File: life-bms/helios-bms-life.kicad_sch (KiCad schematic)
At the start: 55 parts, among them J1 Outboard, J2 Debug, J3 Output, J4 Battery, Q1 SSM6J507NU, Q2 Q_Dual_NMOS_PMOS_S1G1D2S2G2D1, Q3 PMOS, U1 TPSM861253, U2 BQ25306, U3 STM32L011F4Ux, U4 THVD1400D, U5 SIP32434

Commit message: oops screwed up power net labels
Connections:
- net +12V: no longer Q2.4 (S), Q3.3 (D), R17.1
- net VIN: now also Q2.4 (S), Q3.3 (D), R17.1
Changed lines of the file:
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@@
-	)
-	(symbol
-		(lib_id "power:+12V")
-		(at 113.03 125.73 0)
-		(unit 1)
-		(body_style 1)
-		(exclude_from_sim no)
-		(in_bom yes)
-		(on_board yes)
-		(in_pos_files yes)
-		(dnp no)
-		(fields_autoplaced yes)
-		(property "Reference" "#PWR035"
-			(at 113.03 129.54 0)
-			(hide yes)
-			(show_name no)
-			(do_not_autoplace no)
-			(effects
-				(font
-					(size 1.27 1.27)
-				)
-			)
-		)
-		(property "Value" "+12V"
-			(at 113.03 120.65 0)
-			(show_name no)
-			(do_not_autoplace no)
-			(effects
-				(font
-					(size 1.27 1.27)
-				)
-			)
-		)
-		(property "Footprint" ""
-			(at 113.03 125.73 0)
-			(hide yes)
-			(show_name no)
-			(do_not_autoplace no)
-			(effects
-				(font
-					(size 1.27 1.27)
-				)
-			)
-		)
-		(property "Datasheet" ""
-			(at 113.03 125.73 0)
-			(hide yes)
-			(show_name no)
-			(do_not_autoplace no)
-			(effects
-				(font
-					(size 1.27 1.27)
-				)
-			)
-		)
-		(property "Description" "Power symbol creates a global label with name \"+12V\""
-			(at 113.03 125.73 0)
-			(hide yes)
-			(show_name no)
-			(do_not_autoplace no)
-			(effects
-				(font
-					(size 1.27 1.27)
-				)
-			)
-		)
-		(pin "1"
-		)
-		(instances
-			(project "helios-bms-life"
-				(path "/e63e39d7-6ac0-4ffd-8aa3-1841a4541b55"
-					(reference "#PWR035")
-					(unit 1)
-				)
-			)
-		)
 	)
 	(symbol
@@
 					(unit 1)
 				)
+			)
+		)
+	)
+	(symbol
+		(lib_id "power:VBUS")
+		(at 113.03 125.73 0)
+		(unit 1)
+		(body_style 1)
+		(exclude_from_sim no)
+		(in_bom yes)
+		(on_board yes)
+		(in_pos_files yes)
+		(dnp no)
+		(property "Reference" "#PWR035"
+			(at 113.03 129.54 0)
+			(hide yes)
+			(show_name no)
+			(do_not_autoplace no)
+			(effects
+				(font
+					(size 1.27 1.27)
+				)
+			)
+		)
+		(property "Value" "VSYS"
+			(at 113.03 122.174 0)
+			(show_name no)
+			(do_not_autoplace no)
+			(effects
+				(font
+					(size 1.27 1.27)
+				)
+			)
+		)
+		(property "Footprint" ""
+			(at 113.03 125.73 0)
+			(hide yes)
+			(show_name no)
+			(do_not_autoplace no)
+			(effects
+				(font
+					(size 1.27 1.27)
+				)
+			)
+		)
+		(property "Datasheet" ""
+			(at 113.03 125.73 0)
+			(hide yes)
+			(show_name no)
+			(do_not_autoplace no)
+			(effects
+				(font
+					(size 1.27 1.27)
+				)
+			)
+		)
+		(property "Description" "Power symbol creates a global label with name \"VBUS\""
+			(at 113.03 125.73 0)
+			(hide yes)
+			(show_name no)
+			(do_not_autoplace no)
+			(effects
+				(font
+					(size 1.27 1.27)
+				)
+			)
+		)
+		(pin "1"
+		)
+		(instances
+			(project "helios-bms-life"
+				(path "/e63e39d7-6ac0-4ffd-8aa3-1841a4541b55"
+					(reference "#PWR035")
+					(unit 1)
+				)

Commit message: satellite boards done
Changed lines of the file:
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@@
 	)
 	(junction
+		(at 36.83 40.64)
+		(diameter 0)
+		(color 0 0 0 0)
+	)
+	(junction
 		(at 170.18 41.91)
 		(diameter 0)
@@
 	)
 	(junction
+		(at 148.59 48.26)
+		(diameter 0)
+		(color 0 0 0 0)
+	)
+	(junction
 		(at 99.06 102.87)
 		(diameter 0)
@@
 	)
 	(junction
+		(at 19.05 113.03)
+		(diameter 0)
+		(color 0 0 0 0)
+	)
+	(junction
 		(at 36.83 29.21)
 		(diameter 0)
@@
 	)
 	(junction
+		(at 148.59 41.91)
+		(diameter 0)
+		(color 0 0 0 0)
+	)
+	(junction
 		(at 68.58 24.13)
 		(diameter 0)
@@
 	)
 	(junction
+		(at 21.59 24.13)
+		(diameter 0)
+		(color 0 0 0 0)
+	)
+	(junction
 		(at 45.72 130.81)
 		(diameter 0)
@@
 	)
 	(junction
+		(at 96.52 144.78)
+		(diameter 0)
+		(color 0 0 0 0)
+	)
+	(junction
 		(at 30.48 24.13)
 		(diameter 0)
@@
 	)
 	(junction
+		(at 45.72 53.34)
+		(diameter 0)
+		(color 0 0 0 0)
+	)
+	(junction
 		(at 30.48 58.42)
 		(diameter 0)
@@
 		(color 0 0 0 0)
 	)
-	(junction
-		(at 144.78 48.26)
-		(diameter 0)
-		(color 0 0 0 0)
-	)
 	(no_connect
 		(at 31.75 86.36)
@@
 	(wire
 		(pts
-			(xy 30.48 22.86) (xy 30.48 24.13)
+			(xy 21.59 22.86) (xy 21.59 24.13)
 		)
 		(stroke
@@
 	(wire
 		(pts
-			(xy 31.75 111.76) (xy 31.75 113.03)
+			(xy 19.05 111.76) (xy 19.05 113.03)
 		)
 		(stroke
@@
 	(wire
 		(pts
+			(xy 45.72 53.34) (xy 44.45 53.34)
+		)
+		(stroke
+			(width 0)
+			(type default)
+		)
+	)
+	(wire
+		(pts
 			(xy 129.54 90.17) (xy 130.81 90.17)
 		)
@@
 	(wire
 		(pts
+			(xy 148.59 41.91) (xy 161.29 41.91)
+		)
+		(stroke
+			(width 0)
+			(type default)
+		)
+	)
+	(wire
+		(pts
 			(xy 20.32 130.81) (xy 20.32 133.35)
 		)
@@
 	(wire
 		(pts
-			(xy 19.05 113.03) (xy 31.75 113.03)
-		)
-		(stroke
-			(width 0)
-			(type default)
-		)
-	)
-	(wire
-		(pts
 			(xy 91.44 100.33) (xy 91.44 102.87)
 		)
@@
 	(wire
 		(pts
-			(xy 52.07 40.64) (xy 71.12 40.64)
-		)
-		(stroke
-			(width 0)
-			(type default)
-		)
-	)
-	(wire
-		(pts
 			(xy 35.56 175.26) (xy 43.18 175.26)
 		)
@@
 	(wire
 		(pts
-			(xy 85.09 144.78) (xy 85.09 146.05)
+			(xy 96.52 144.78) (xy 96.52 147.32)
 		)
 		(stroke
@@
 	(wire
 		(pts
-			(xy 138.43 48.26) (xy 144.78 48.26)
+			(xy 138.43 48.26) (xy 148.59 48.26)
 		)
 		(stroke
@@
 	(wire
 		(pts
-			(xy 144.78 41.91) (xy 144.78 48.26)
+			(xy 148.59 41.91) (xy 148.59 48.26)
 		)
 		(stroke
@@
 	(wire
 		(pts
-			(xy 46.99 53.34) (xy 44.45 53.34)
+			(xy 46.99 53.34) (xy 45.72 53.34)
 		)
 		(stroke
@@
 	(wire
 		(pts
-			(xy 144.78 41.91) (xy 161.29 41.91)
-		)
-		(stroke
-			(width 0)
-			(type default)
-		)
-	)
-	(wire
-		(pts
 			(xy 36.83 24.13) (xy 39.37 24.13)
 		)
@@
 	(wire
 		(pts
-			(xy 36.83 40.64) (xy 52.07 40.64)
+			(xy 36.83 40.64) (xy 71.12 40.64)
 		)
 		(stroke
@@
 	(wire
 		(pts
+			(xy 148.59 41.91) (xy 144.78 41.91)
+		)
+		(stroke
+			(width 0)
+			(type default)
+		)
+	)
+	(wire
+		(pts
 			(xy 138.43 62.23) (xy 138.43 60.96)
 		)
@@
 	(wire
 		(pts
+			(xy 19.05 113.03) (xy 31.75 113.03)
+		)
+		(stroke
+			(width 0)
+			(type default)
+		)
+	)
+	(wire
+		(pts
 			(xy 57.15 71.12) (xy 59.69 71.12)
 		)
@@
 	(wire
 		(pts
-			(xy 148.59 48.26) (xy 144.78 48.26)
-		)
-		(stroke
-			(width 0)
-			(type default)
-		)
-	)
-	(wire
-		(pts
 			(xy 121.92 69.85) (xy 121.92 71.12)
 		)
@@
 	(wire
 		(pts
-			(xy 44.45 52.07) (xy 44.45 53.34)
+			(xy 45.72 52.07) (xy 45.72 53.34)
 		)
 		(stroke
@@
 	(symbol
 		(lib_id "power:GND")
-		(at 52.07 40.64 0)
+		(at 36.83 40.64 0)
 		(unit 1)
 		(body_style 1)
@@
 		(dnp no)
 		(property "Reference" "#PWR08"
-			(at 52.07 46.99 0)
+			(at 36.83 46.99 0)
 			(hide yes)
 			(show_name no)
@@
 		)
 		(property "Value" "GND"
-			(at 52.07 44.45 0)
+			(at 36.83 44.45 0)
 			(show_name no)
 			(do_not_autoplace no)
@@
 		)
 		(property "Footprint" ""
-			(at 52.07 40.64 0)
+			(at 36.83 40.64 0)
 			(hide yes)
 			(show_name no)
@@
 		)
 		(property "Datasheet" ""
-			(at 52.07 40.64 0)
+			(at 36.83 40.64 0)
 			(hide yes)
 			(show_name no)
@@
 		)
 		(property "Description" "Power symbol creates a global label with name \"GND\" , ground"
-			(at 52.07 40.64 0)
+			(at 36.83 40.64 0)
 			(hide yes)
 			(show_name no)
@@
 	(symbol
 		(lib_id "power:+12V")
-		(at 30.48 22.86 0)
+		(at 21.59 22.86 0)
 		(unit 1)
 		(body_style 1)
@@
 		(fields_autoplaced yes)
 		(property "Reference" "#PWR02"
-			(at 30.48 26.67 0)
+			(at 21.59 26.67 0)
 			(hide yes)
 			(show_name no)
@@
 		)
 		(property "Value" "+12V"
-			(at 30.48 17.78 0)
+			(at 21.59 17.78 0)
 			(show_name no)
 			(do_not_autoplace no)
@@
 		)
 		(property "Footprint" ""
-			(at 30.48 22.86 0)
+			(at 21.59 22.86 0)
 			(hide yes)
 			(show_name no)
@@
 		)
 		(property "Datasheet" ""
-			(at 30.48 22.86 0)
+			(at 21.59 22.86 0)
 			(hide yes)
 			(show_name no)
@@
 		)
 		(property "Description" "Power symbol creates a global label with name \"+12V\""
-			(at 30.48 22.86 0)
+			(at 21.59 22.86 0)
 			(hide yes)
 			(show_name no)
@@
 	(symbol
 		(lib_id "power:+3.3V")
-		(at 31.75 111.76 0)
+		(at 19.05 111.76 0)
 		(unit 1)
 		(body_style 1)
@@
 		(dnp no)
 		(property "Reference" "#PWR023"
-			(at 31.75 115.57 0)
+			(at 19.05 115.57 0)
 			(hide yes)
 			(show_name no)
@@
 		)
 		(property "Value" "+3.3V"
-			(at 31.75 108.458 0)
+			(at 19.05 108.458 0)
 			(show_name no)
 			(do_not_autoplace no)
@@
 		)
 		(property "Footprint" ""
-			(at 31.75 111.76 0)
+			(at 19.05 111.76 0)
 			(hide yes)
 			(show_name no)
@@
 		)
 		(property "Datasheet" ""
-			(at 31.75 111.76 0)
+			(at 19.05 111.76 0)
 			(hide yes)
 			(show_name no)
@@
 		)
 		(property "Description" "Power symbol creates a global label with name \"+3.3V\""
-			(at 31.75 111.76 0)
+			(at 19.05 111.76 0)
 			(hide yes)
 			(show_name no)
@@
 	(symbol
 		(lib_id "power:+3.3V")
-		(at 44.45 52.07 0)
+		(at 45.72 52.07 0)
 		(unit 1)
 		(body_style 1)
@@
 		(dnp no)
 		(property "Reference" "#PWR011"
-			(at 44.45 55.88 0)
+			(at 45.72 55.88 0)
 			(hide yes)
 			(show_name no)
@@
 		)
 		(property "Value" "+3.3V"
-			(at 44.45 48.514 0)
+			(at 45.72 48.514 0)
 			(show_name no)
 			(do_not_autoplace no)
@@
 		)
 		(property "Footprint" ""
-			(at 44.45 52.07 0)
+			(at 45.72 52.07 0)
 			(hide yes)
 			(show_name no)
@@
 		)
 		(property "Datasheet" ""
-			(at 44.45 52.07 0)
+			(at 45.72 52.07 0)
 			(hide yes)
 			(show_name no)
@@
 		)
 		(property "Description" "Power symbol creates a global label with name \"+3.3V\""
-			(at 44.45 52.07 0)
+			(at 45.72 52.07 0)
 			(hide yes)
 			(show_name no)
@@
 	(symbol
 		(lib_id "power:GND")
-		(at 85.09 146.05 0)
+		(at 96.52 147.32 0)
 		(unit 1)
 		(body_style 1)
@@
 		(fields_autoplaced yes)
 		(property "Reference" "#PWR029"
-			(at 85.09 152.4 0)
+			(at 96.52 153.67 0)
 			(hide yes)
 			(show_name no)
@@
 		)
 		(property "Value" "GND"
-			(at 85.09 151.13 0)
+			(at 96.52 152.4 0)
 			(show_name no)
 			(do_not_autoplace no)
@@
 		)
 		(property "Footprint" ""
-			(at 85.09 146.05 0)
+			(at 96.52 147.32 0)
 			(hide yes)
 			(show_name no)
@@
 		)
 		(property "Datasheet" ""
-			(at 85.09 146.05 0)
+			(at 96.52 147.32 0)
 			(hide yes)
 			(show_name no)
@@
 		)
 		(property "Description" "Power symbol creates a global label with name \"GND\" , ground"
-			(at 85.09 146.05 0)
+			(at 96.52 147.32 0)
 			(hide yes)
 			(show_name no)

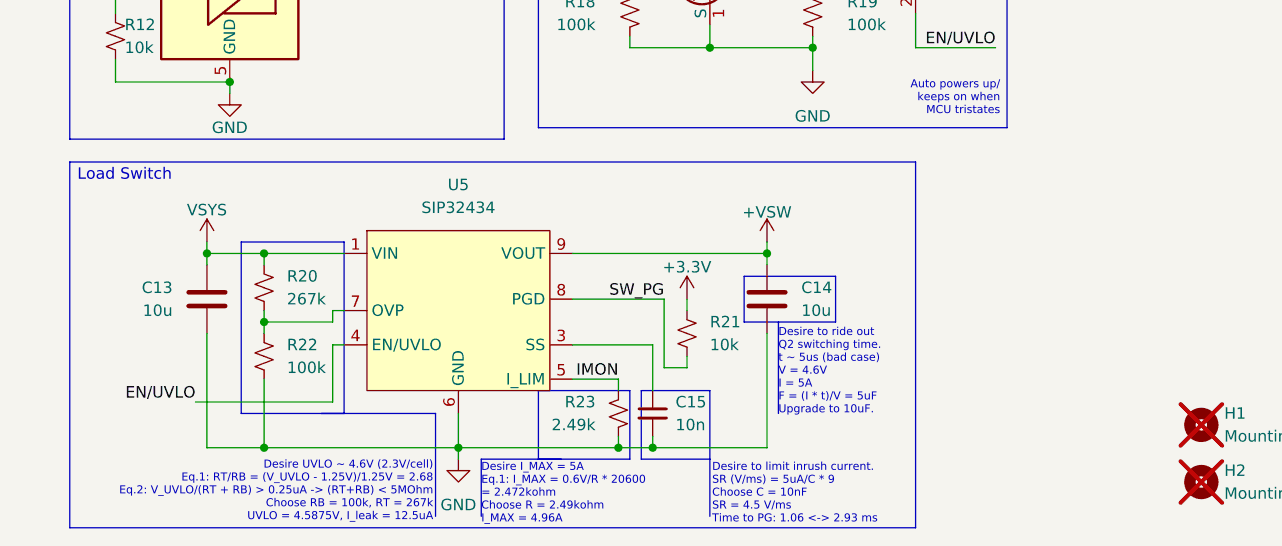
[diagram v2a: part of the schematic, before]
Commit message: BMS satellite boards ready, controller needs routing
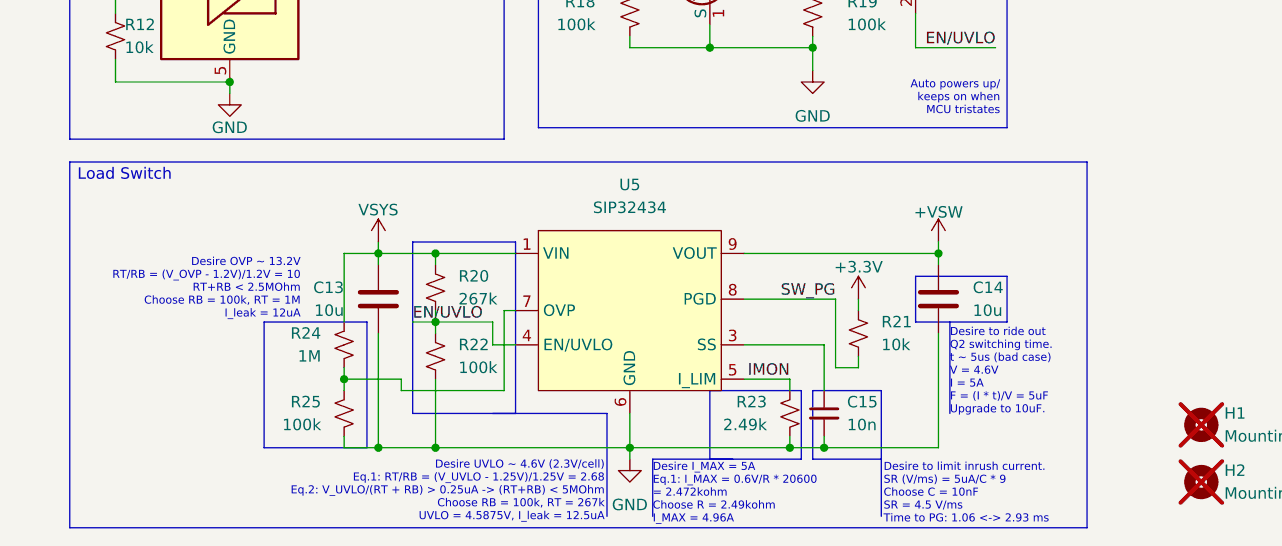
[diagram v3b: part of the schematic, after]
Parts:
- added R24: 1M, Resistor_SMD:R_0402_1005Metric, symbol Device:R_Small_US
- added R25: 100k, Resistor_SMD:R_0402_1005Metric, symbol Device:R_Small_US
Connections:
- net EN/UVLO: now also R20.1, R22.2
- net GND: now also R25.1
- net VIN: now also R24.2
- new net: R24.1, R25.2, U5.7 (OVP)
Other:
- note added: "Desire OVP ~ 13.2V RT/RB = (V_OVP - 1.2V)/1.2V = 10 RT+RB < 2.5MOhm Choose RB = 100k, RT = 1M I_leak = 12uA"
- moved on the sheet: C13, C14, C15, R20, R21, R22, R23, U5
